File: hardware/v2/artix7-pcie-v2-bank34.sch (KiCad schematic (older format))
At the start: 2 parts, among them J6 Conn_02x20_Odd_Even, U1 XC7A75T-FGG484

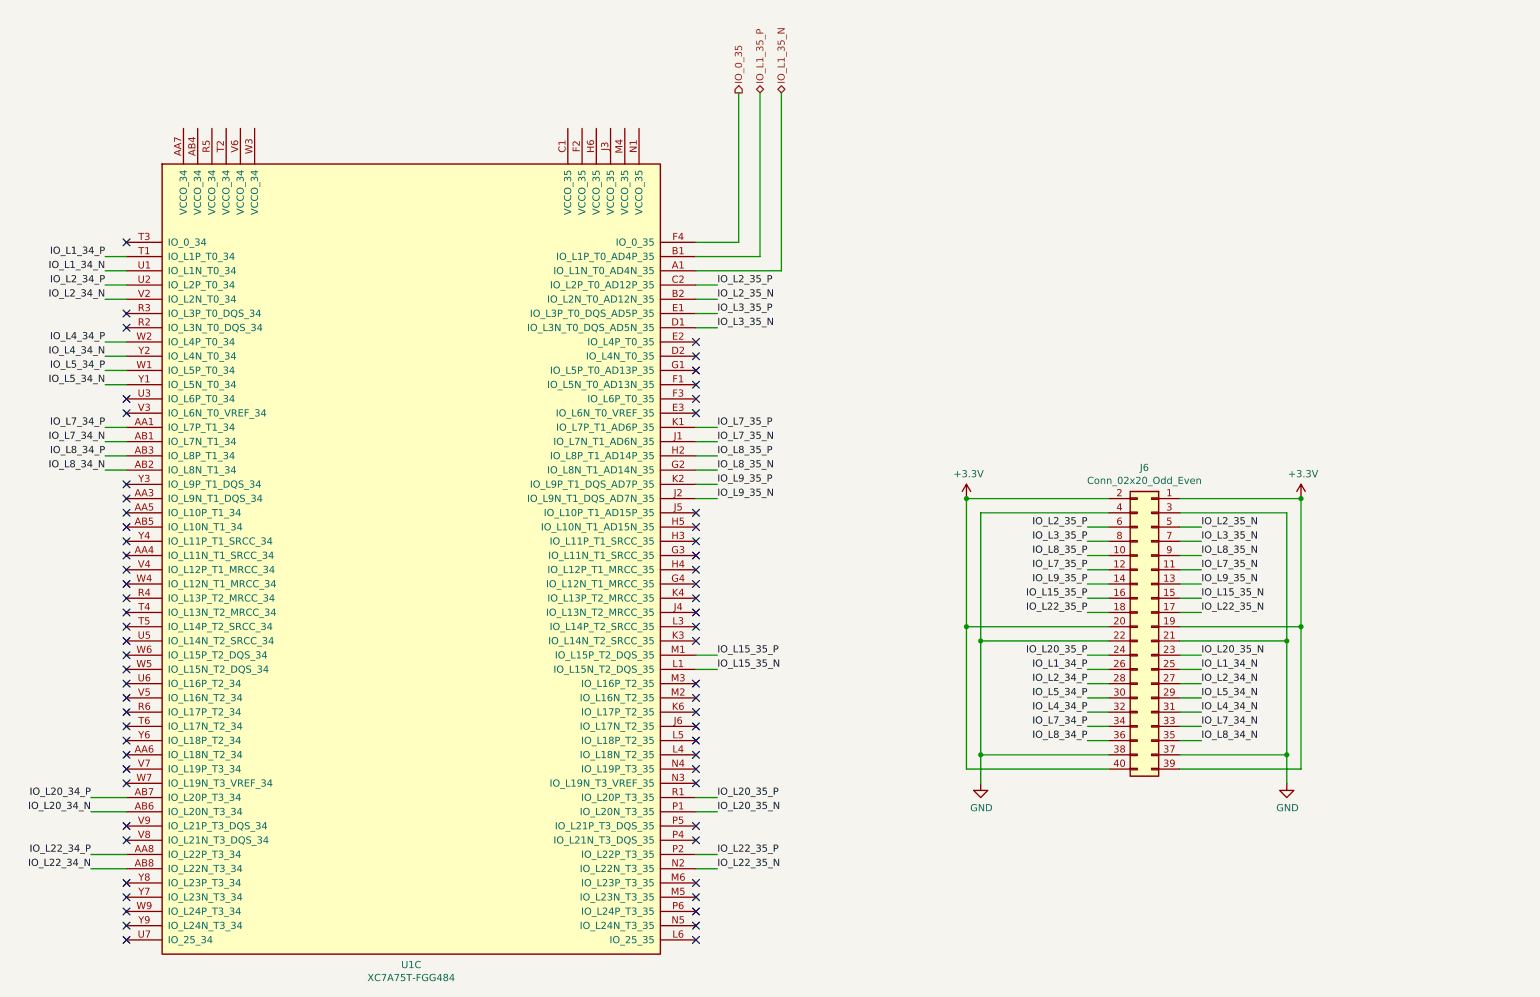
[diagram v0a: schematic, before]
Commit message: v2 schematic/pcb: band 13 to NC for smaller device compatibility
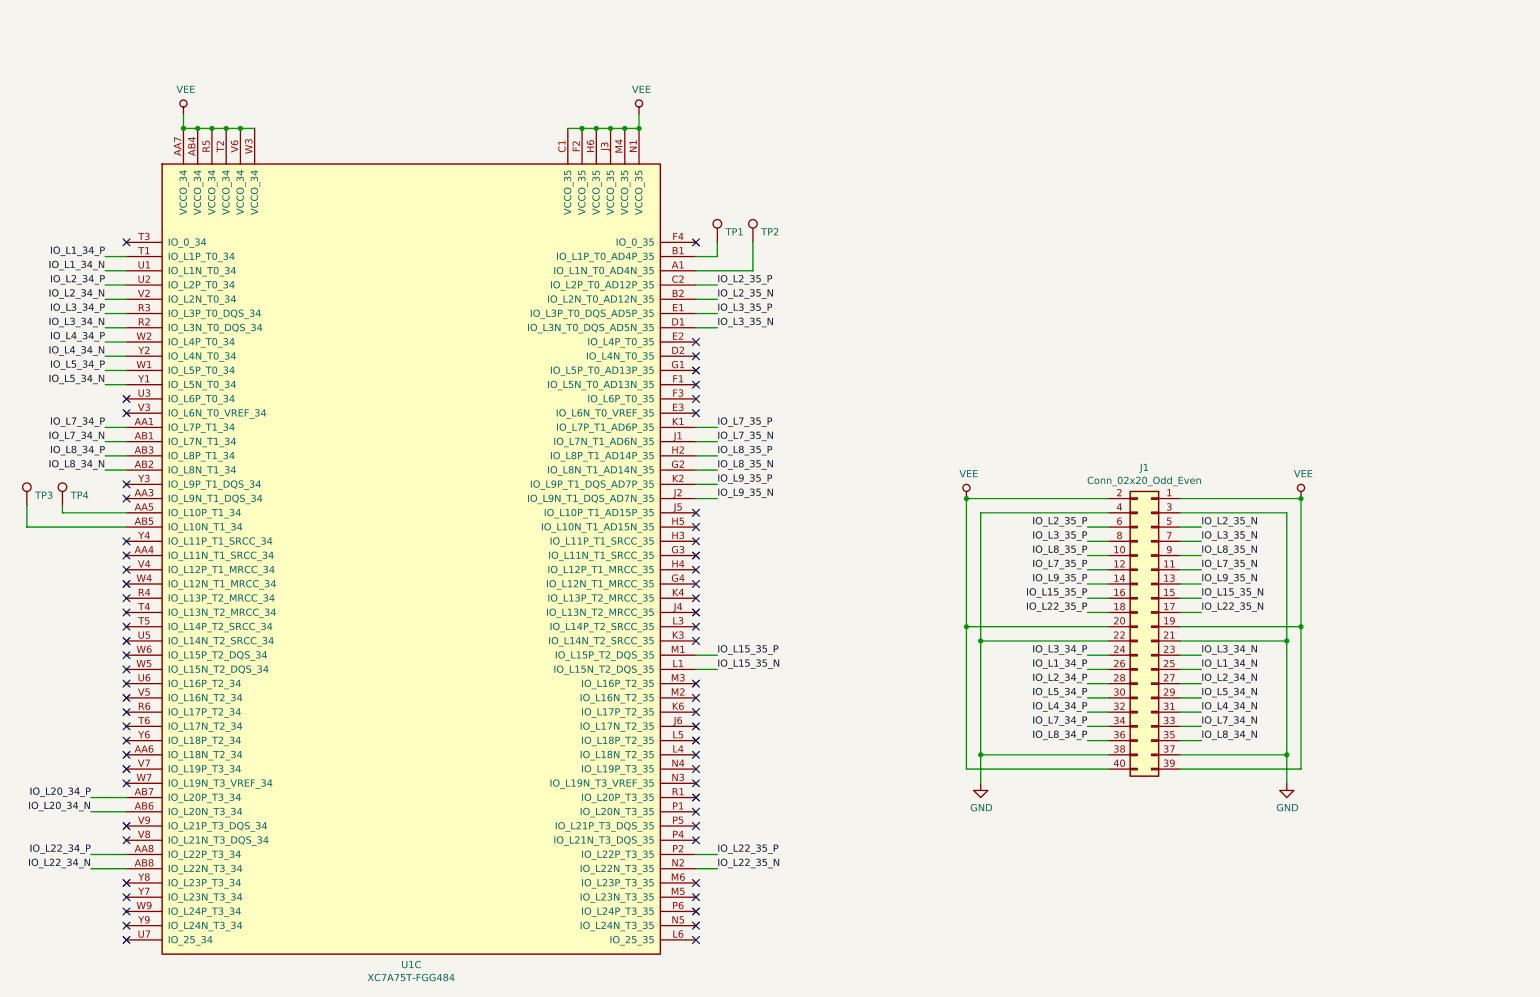
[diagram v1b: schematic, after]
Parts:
- added TP1, TP2, TP3, TP4: TestPoint, tom-mechanical:TestPoint_Pad_D1.5mm, symbol tom-mechanical:TestPoint
- renumbered J6 to J1
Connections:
- net +3V3 is gone; now on net VEE: J1.1 (Pin_1), J1.19 (Pin_19), J1.2 (Pin_2), J1.20 (Pin_20), J1.39 (Pin_39), J1.40 (Pin_40)
- net at U1.AA5 (IO_L10P_T1_34): now also TP4.1
- net VEE: now reaches U1.AA7 (VCCO_34)
- net VEE: now also U1.AB4 (VCCO_34), U1.C1 (VCCO_35), U1.F2 (VCCO_35), U1.H6 (VCCO_35), U1.J3 (VCCO_35), U1.M4 (VCCO_35), U1.N1 (VCCO_35), U1.R5 (VCCO_34), U1.T2 (VCCO_34), U1.V6 (VCCO_34), U1.W3 (VCCO_34)
- net at U1.AB5 (IO_L10N_T1_34): now also TP3.1
- net IO_L3_34_N: now reaches U1.R2 (IO_L3N_T0_DQS_34)
- net IO_L3_34_N: now also J1.23 (Pin_23)
- net IO_L3_34_P: now reaches U1.R3 (IO_L3P_T0_DQS_34)
- net IO_L3_34_P: now also J1.24 (Pin_24)
- net IO_0_35: no longer names the net of U1.F4 (IO_0_35)
- net IO_L1_35_N: no longer names the net of U1.A1 (IO_L1N_T0_AD4N_35)
- net IO_L1_35_N: now also TP2.1
- net IO_L1_35_P: no longer names the net of U1.B1 (IO_L1P_T0_AD4P_35)
- net IO_L1_35_P: now also TP1.1
- net IO_L20_35_N: no longer names the net of U1.P1 (IO_L20N_T3_35)
- net IO_L20_35_N: no longer J1.23 (Pin_23)
- net IO_L20_35_P: no longer names the net of U1.R1 (IO_L20P_T3_35)
- net IO_L20_35_P: no longer J1.24 (Pin_24)
- no-connect marks 65 -> 64
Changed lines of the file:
@@
 $Descr A4 11693 8268
 encoding utf-8
-Sheet 5 6
+Sheet 7 7
 Title ""
 Date ""
@@
 P 8500 4750
 AR Path="/5E5E2B54/5E70D5E0" Ref="J?"  Part="1"
-AR Path="/5E6D5E13/5E70D5E0" Ref="J6"  Part="1"
-F 0 "J6" H 8550 5867 50  0000 C CNN
+AR Path="/5E6D5E13/5E70D5E0" Ref="J1"  Part="1"
+F 0 "J1" H 8550 5867 50  0000 C CNN
 F 1 "Conn_02x20_Odd_Even" H 8550 5776 50  0000 C CNN
 F 2 "artix7-pcie-v2:Socket_Strip_Angled_2x20" H 8500 4750 50  0001 C CNN
@@
 	-1   0    0    -1
 $EndComp
-$Comp
-L power:+3.3V #PWR?
-U 1 1 5E70D5E6
-P 9550 3850
-AR Path="/5E5E2B54/5E70D5E6" Ref="#PWR?"  Part="1"
-AR Path="/5E6D5E13/5E70D5E6" Ref="#PWR0101"  Part="1"
-F 0 "#PWR0101" H 9550 3700 50  0001 C CNN
-F 1 "+3.3V" H 9565 4023 50  0000 C CNN
-F 2 "" H 9550 3850 50  0001 C CNN
-F 3 "" H 9550 3850 50  0001 C CNN
-	1    9550 3850
-	1    0    0    -1
-$EndComp
-$Comp
-L power:+3.3V #PWR?
-U 1 1 5E70D5EC
-P 7200 3850
-AR Path="/5E5E2B54/5E70D5EC" Ref="#PWR?"  Part="1"
-AR Path="/5E6D5E13/5E70D5EC" Ref="#PWR0102"  Part="1"
-F 0 "#PWR0102" H 7200 3700 50  0001 C CNN
-F 1 "+3.3V" H 7215 4023 50  0000 C CNN
-F 2 "" H 7200 3850 50  0001 C CNN
-F 3 "" H 7200 3850 50  0001 C CNN
-	1    7200 3850
-	1    0    0    -1
-$EndComp
 Wire Wire Line
 	8700 3850 9550 3850
@@
 Wire Wire Line
 	9550 4750 9550 3850
-Connection ~ 9550 3850
 Wire Wire Line
 	8200 4750 7200 4750
 Wire Wire Line
 	7200 4750 7200 3850
-Connection ~ 7200 3850
 Wire Wire Line
 	8700 5750 9550 5750
@@
 Wire Wire Line
 	7300 4850 7300 3950
-Text HLabel 5750 1000 1    50   BiDi ~ 0
-IO_L1_35_P
-Text HLabel 5900 1000 1    50   BiDi ~ 0
-IO_L1_35_N
-Wire Wire Line
-	5300 2150 5750 2150
-Wire Wire Line
-	5750 2150 5750 1000
-Wire Wire Line
-	5300 2250 5900 2250
-Wire Wire Line
-	5900 2250 5900 1000
-Text HLabel 5600 1000 1    50   Output ~ 0
-IO_0_35
 Wire Wire Line
 	1050 5950 1300 5950
@@
 	1300 3650 1150 3650
 Wire Wire Line
-	5300 2050 5600 2050
-Wire Wire Line
-	5600 2050 5600 1000
-Wire Wire Line
 	8050 4050 8200 4050
 Wire Wire Line
@@
 Wire Wire Line
 	5450 2450 5300 2450
-Wire Wire Line
-	5450 6050 5300 6050
-Wire Wire Line
-	5300 5950 5450 5950
 Wire Wire Line
 	5450 6450 5300 6450
@@
 Text Label 5450 6450 0    50   ~ 0
 IO_L22_35_N
-Text Label 5450 5950 0    50   ~ 0
-IO_L20_35_P
-Text Label 5450 6050 0    50   ~ 0
-IO_L20_35_N
 Text Label 8050 4050 2    50   ~ 0
 IO_L2_35_P
@@
 Text Label 8050 4650 2    50   ~ 0
 IO_L22_35_P
-Text Label 8050 4950 2    50   ~ 0
-IO_L20_35_P
 Text Label 8050 5050 2    50   ~ 0
 IO_L1_34_P
@@
 Text Label 8850 4650 0    50   ~ 0
 IO_L22_35_N
-Text Label 8850 4950 0    50   ~ 0
-IO_L20_35_N
 Text Label 8850 5050 0    50   ~ 0
 IO_L1_34_N
@@
 NoConn ~ 1300 4250
 NoConn ~ 1300 4150
-NoConn ~ 1300 4050
-NoConn ~ 1300 3950
 NoConn ~ 1300 3850
 NoConn ~ 1300 3750
 NoConn ~ 1300 3250
 NoConn ~ 1300 3150
-NoConn ~ 1300 2650
-NoConn ~ 1300 2550
 NoConn ~ 1300 2050
+Wire Wire Line
+	4400 1250 4500 1250
+Connection ~ 4500 1250
+Wire Wire Line
+	4500 1250 4600 1250
+Connection ~ 4600 1250
+Wire Wire Line
+	4600 1250 4700 1250
+Connection ~ 4700 1250
+Wire Wire Line
+	4700 1250 4800 1250
+Connection ~ 4800 1250
+Wire Wire Line
+	4800 1250 4900 1250
+Wire Wire Line
+	4900 1250 4900 1150
+Connection ~ 4900 1250
+Wire Wire Line
+	2200 1250 2100 1250
+Connection ~ 1800 1250
+Wire Wire Line
+	1800 1250 1700 1250
+Connection ~ 1900 1250
+Wire Wire Line
+	1900 1250 1800 1250
+Connection ~ 2000 1250
+Wire Wire Line
+	2000 1250 1900 1250
+Connection ~ 2100 1250
+Wire Wire Line
+	2100 1250 2000 1250
+Wire Wire Line
+	1700 1250 1700 1150
+Connection ~ 1700 1250
+NoConn ~ 5300 2050
+$Comp
+L tom-mechanical:TestPoint TP1
+U 1 1 5F37E446
+P 5450 2050
+F 0 "TP1" H 5508 2122 50  0000 L CNN
+F 1 "TestPoint" H 5508 2077 50  0001 L CNN
+F 2 "tom-mechanical:TestPoint_Pad_D1.5mm" H 5650 2050 50  0001 C CNN
+F 3 "~" H 5650 2050 50  0001 C CNN
+	1    5450 2050
+	1    0    0    -1
+$EndComp
+$Comp
+L tom-mechanical:TestPoint TP2
+U 1 1 5F37EBC2
+P 5700 2050
+F 0 "TP2" H 5758 2122 50  0000 L CNN
+F 1 "TestPoint" H 5758 2077 50  0001 L CNN
+F 2 "tom-mechanical:TestPoint_Pad_D1.5mm" H 5900 2050 50  0001 C CNN
+F 3 "~" H 5900 2050 50  0001 C CNN
+	1    5700 2050
+	1    0    0    -1
+$EndComp
+Wire Wire Line
+	5450 2050 5450 2150
+Wire Wire Line
+	5450 2150 5300 2150
+Wire Wire Line
+	5300 2250 5700 2250
+Wire Wire Line
+	5700 2250 5700 2050
+$Comp
+L tom-mechanical:TestPoint TP4
+U 1 1 5F392D5A
+P 850 3900
+F 0 "TP4" H 908 3972 50  0000 L CNN
+F 1 "TestPoint" H 908 3927 50  0001 L CNN
+F 2 "tom-mechanical:TestPoint_Pad_D1.5mm" H 1050 3900 50  0001 C CNN
+F 3 "~" H 1050 3900 50  0001 C CNN
+	1    850  3900
+	1    0    0    -1
+$EndComp
+Wire Wire Line
+	1300 3950 850  3950
+Wire Wire Line
+	850  3950 850  3900
+Wire Wire Line
+	600  3900 600  4050
+Wire Wire Line
+	600  4050 1300 4050
+$Comp
+L tom-mechanical:TestPoint TP3
+U 1 1 5F39221C
+P 600 3900
+F 0 "TP3" H 658 3972 50  0000 L CNN
+F 1 "TestPoint" H 658 3927 50  0001 L CNN
+F 2 "tom-mechanical:TestPoint_Pad_D1.5mm" H 800 3900 50  0001 C CNN
+F 3 "~" H 800 3900 50  0001 C CNN
+	1    600  3900
+	1    0    0    -1
+$EndComp
+$Comp
+L power:VEE #PWR0126
+U 1 1 5F4DD67C
+P 1700 1150
+F 0 "#PWR0126" H 1700 1000 50  0001 C CNN
+F 1 "VEE" H 1717 1323 50  0000 C CNN
+F 2 "" H 1700 1150 50  0001 C CNN
+F 3 "" H 1700 1150 50  0001 C CNN
+	1    1700 1150
+	1    0    0    -1
+$EndComp
+$Comp
+L power:VEE #PWR0127
+U 1 1 5F4E04F5
+P 4900 1150
+F 0 "#PWR0127" H 4900 1000 50  0001 C CNN
+F 1 "VEE" H 4917 1323 50  0000 C CNN
+F 2 "" H 4900 1150 50  0001 C CNN
+F 3 "" H 4900 1150 50  0001 C CNN
+	1    4900 1150
+	1    0    0    -1
+$EndComp
+$Comp
+L power:VEE #PWR0128
+U 1 1 5F4E5BA1
+P 9550 3850
+F 0 "#PWR0128" H 9550 3700 50  0001 C CNN
+F 1 "VEE" H 9567 4023 50  0000 C CNN
+F 2 "" H 9550 3850 50  0001 C CNN
+F 3 "" H 9550 3850 50  0001 C CNN
+	1    9550 3850
+	1    0    0    -1
+$EndComp
+Connection ~ 9550 3850
+$Comp
+L power:VEE #PWR0129
+U 1 1 5F4E5DA1
+P 7200 3850
+F 0 "#PWR0129" H 7200 3700 50  0001 C CNN
+F 1 "VEE" H 7217 4023 50  0000 C CNN
+F 2 "" H 7200 3850 50  0001 C CNN
+F 3 "" H 7200 3850 50  0001 C CNN
+	1    7200 3850
+	1    0    0    -1
+$EndComp
+Connection ~ 7200 3850
+Wire Wire Line
+	1300 2550 1150 2550
+Wire Wire Line
+	1300 2650 1150 2650
+Text Label 1150 2550 2    50   ~ 0
+IO_L3_34_P
+Text Label 1150 2650 2    50   ~ 0
+IO_L3_34_N
+NoConn ~ 5300 6050
+NoConn ~ 5300 5950
+Text Label 8050 4950 2    50   ~ 0
+IO_L3_34_P
+Text Label 8850 4950 0    50   ~ 0
+IO_L3_34_N
 $EndSCHEMATC
